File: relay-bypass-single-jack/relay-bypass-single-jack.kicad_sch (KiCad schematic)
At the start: 46 parts, among them J2 8, J4 3, Q2 DMP3099L, Q3 DMN62D0U-7, U1 STM32C011F4Ux, U3 TLV76701DRVR

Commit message: Added second project for exploring a single-jack side mounted version
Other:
- note removed: "TODO change to LDO that's stable w/ low ESR?"
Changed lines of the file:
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@@
 		)
 	)
-	(text "TODO change to LDO that's stable w/ low ESR?"
-		(exclude_from_sim no)
-		(at 131.445 29.21 0)
-		(effects
-			(font
-				(size 1.27 1.27)
-				(color 132 0 0 1)
-			)
-		)
-	)
 	(text "Reverse Polarity\nProtection"
 		(exclude_from_sim no)
@@
 		)
 		(instances
-			(project "relay-bypass"
+			(project "relay-bypass-single-jack"
 				(path "/1a8abc1e-f066-401c-b73c-6efc7ca39ffd"
 					(page "3")

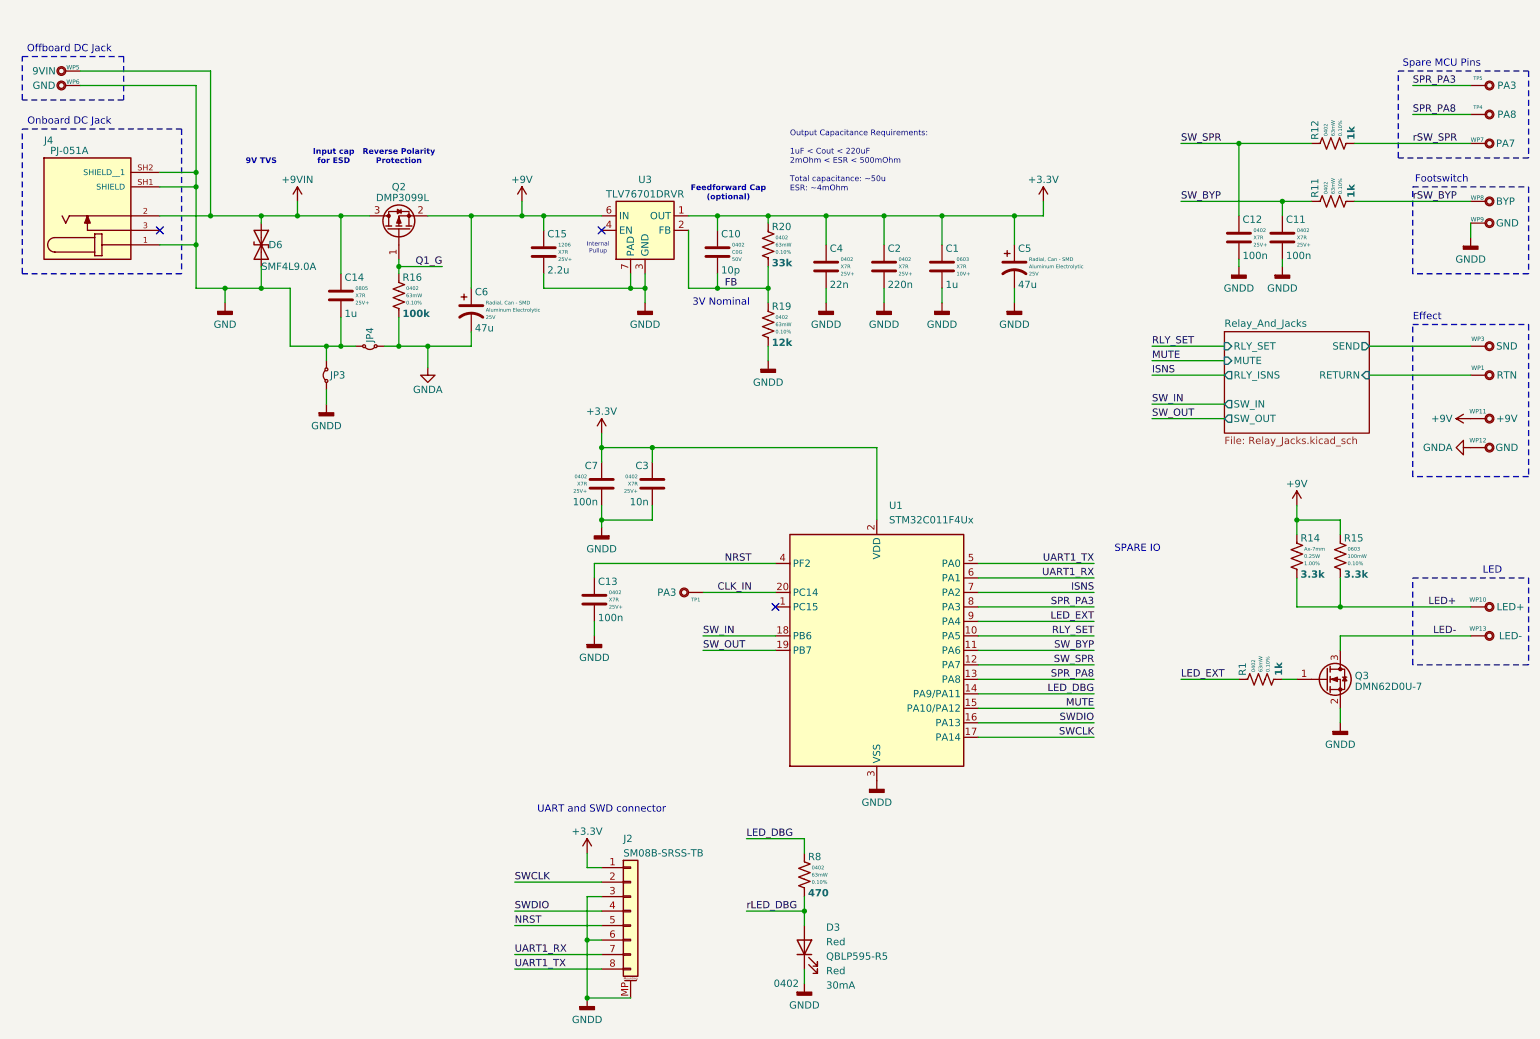
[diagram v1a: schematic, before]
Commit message: Pivoted to dual-jack version on opposing sides.
125B only, using "innie" jacks. Solder-in-place.
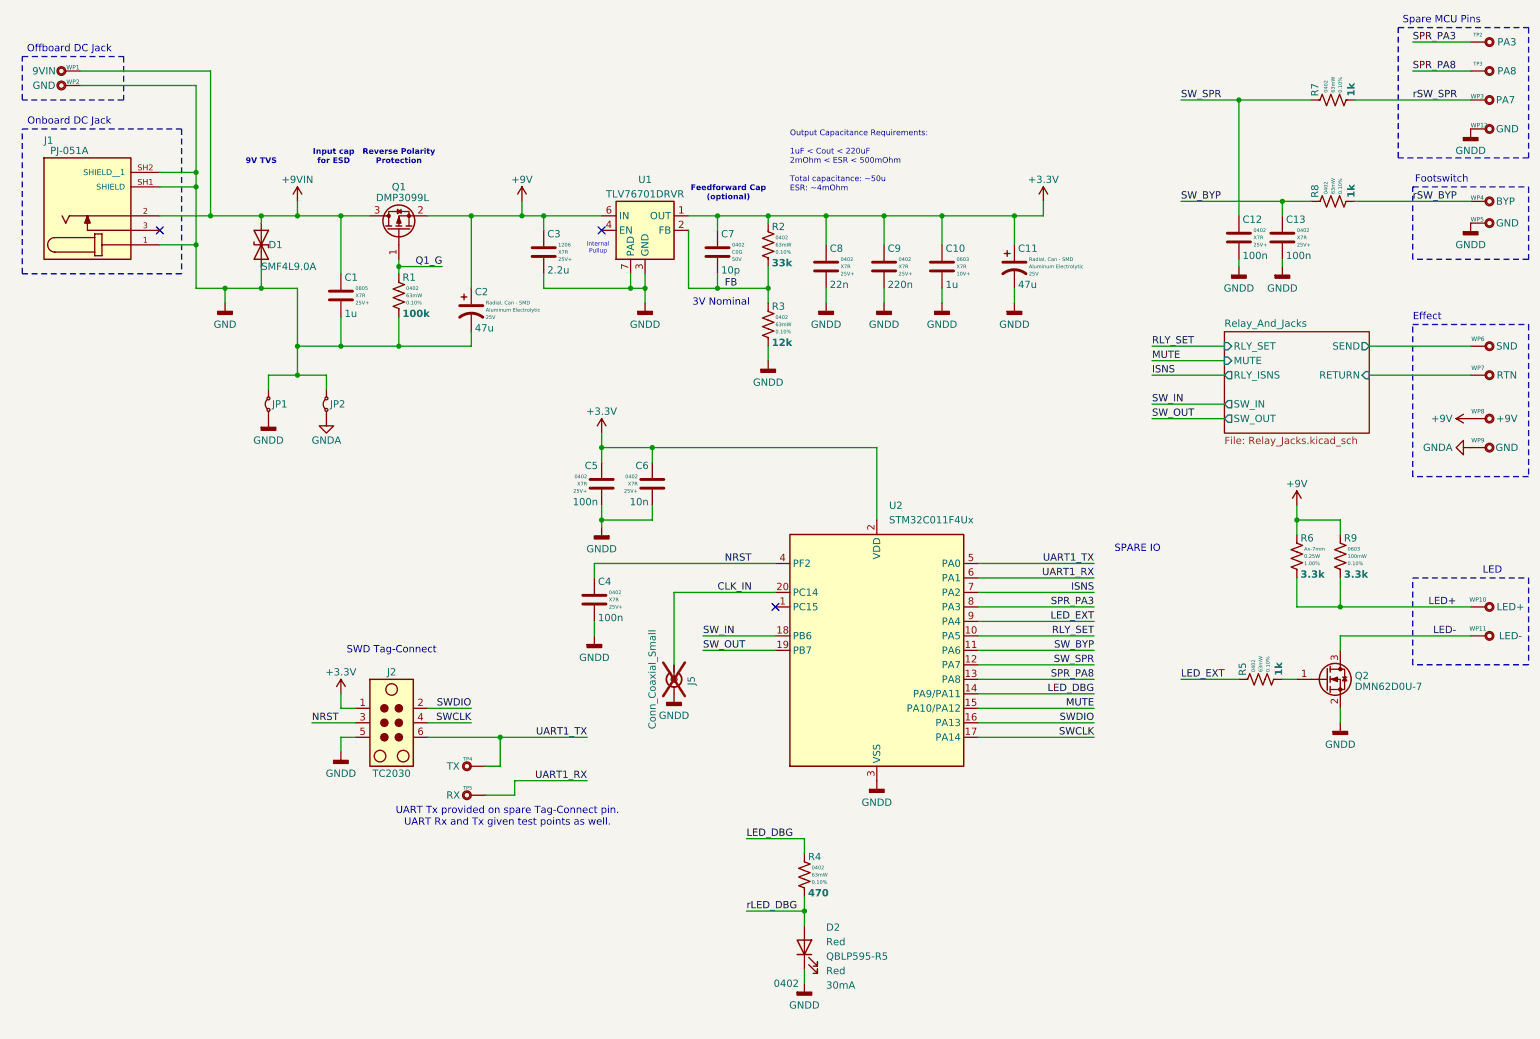
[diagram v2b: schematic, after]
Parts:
- removed J2: 8, Connector_JST:JST_SH_BM08B-SRSS-TB_1x08-1MP_P1.00mm_Vertical, symbol #gplm:con/CON-5001-0008
- removed TP1: PA3, g-art:TestPoint_PTH_H1.02mm_NoOutline, symbol #gplm:art/ART-0000-N102
- added J2: TC2030, Connector:Tag-Connect_TC2030-IDC-NL_2x03_P1.27mm_Vertical, symbol Connector:TC2030
- added J5: Conn_Coaxial_Small, Connector_Coaxial:U.FL_Hirose_U.FL-R-SMT-1_Vertical, symbol Connector:Conn_Coaxial_Small
- added TP4: TX, g-art:TestPoint_PTH_H1.02mm_NoOutline, symbol #gplm:art/ART-0000-N102
- added TP5: RX, g-art:TestPoint_PTH_H1.02mm_NoOutline, symbol #gplm:art/ART-0000-N102
- added WP12: GND, g-art:WirePad_H0.95mm_22-24AWG, symbol #gplm:art/ART-1001-0P95
- renumbered C14 to C1, C1 to C10, C5 to C11, C11 to C13, C6 to C2, C15 to C3, C13 to C4, C7 to C5, C3 to C6, C10 to C7, C4 to C8, C2 to C9, D6 to D1, D3 to D2, J4 to J1, JP3 to JP1, JP4 to JP2, Q2 to Q1, Q3 to Q2, R16 to R1, R20 to R2, R19 to R3, R8 to R4, R1 to R5, R14 to R6, R12 to R7, R11 to R8, R15 to R9, TP5 to TP2, TP4 to TP3, U3 to U1, U1 to U2, WP5 to WP1, WP13 to WP11, WP6 to WP2, WP7 to WP3, WP8 to WP4, WP9 to WP5, WP3 to WP6, WP1 to WP7, WP11 to WP8, WP12 to WP9
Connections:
- net +3.3V: now also J2.1
- net CLK_IN: now also J5.1 (In)
- net GND: now also C2.2, R1.2
- net GNDA: no longer C2.2, R1.2
- net GNDD: now also J2.5, J5.2 (Ext), WP12.1
- net NRST: now also J2.3
- net SWCLK: now also J2.4
- net SWDIO: now also J2.2
- net UART1_RX: now also TP5.1
- net UART1_TX: now also J2.6, TP4.1
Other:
- note added: "SWD Tag-Connect"
- note added: "UART Tx provided on spare Tag-Connect pin. UART Rx and Tx given test points as well."
- note removed: "UART and SWD connector"
- moved on the sheet: JP1, JP2, R7, TP2, TP3, WP3

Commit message: Scratchwork
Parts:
- removed C11: 47u, Capacitor_SMD:CP_Elec_6.3x5.8, symbol #gplm:cap/CAP-3005-047U
- added C11, C17: 100n, Capacitor_SMD:C_0402_1005Metric, symbol #gplm:cap/CAP-4103-100N
- added C16: 4.7u, Capacitor_SMD:C_1206_3216Metric, symbol #gplm:cap/CAP-4106-04U7
- added U4: LM317LCPK, Package_TO_SOT_SMD:SOT-223, symbol #gplm:reg/REG-1011-0ADJ
- C10: footprint Capacitor_SMD:C_0603_1608Metric -> Capacitor_SMD:C_0805_2012Metric; symbol #gplm:cap/CAP-4107-001U -> #gplm:cap/CAP-4105-001U; IPN CAP-4107-001U -> CAP-4105-001U; MPN C0603C105K8RACTU -> C0805C105K3RACTU; Package/Case 0603 -> 805; Voltage 10V+ -> 25V+
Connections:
- net +3.3V: now also C16.1, C17.1, U4.2 (VO), U4.4 (VO)
- net +9V: now also C11.1, U4.3 (VI)
- net FB: now also U4.1 (GND)
- net GNDD: now also C11.2, C16.2, C17.2
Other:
- moved on the sheet: C3
